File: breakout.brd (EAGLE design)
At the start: 25.4 x 32.4 mm, 11 parts, among them IC2 REG1117

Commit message: Tidy up for publishing
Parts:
- added FRAME1: (no value), SparkFun-Aesthetics:DUMMY
- added LOGO1: OSHW-LOGOS, SparkFun-Aesthetics:OSHW-LOGO-S
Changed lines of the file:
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@@
 <layer number="112" name="tSilk" color="7" fill="1" visible="yes" active="yes"/>
 <layer number="113" name="IDFDebug" color="4" fill="1" visible="yes" active="yes"/>
+<layer number="114" name="FRNTMAAT1" color="7" fill="1" visible="yes" active="yes"/>
+<layer number="115" name="FRNTMAAT2" color="7" fill="1" visible="yes" active="yes"/>
 <layer number="116" name="Patch_BOT" color="9" fill="4" visible="no" active="yes"/>
+<layer number="117" name="BACKMAAT1" color="7" fill="1" visible="yes" active="yes"/>
+<layer number="118" name="Rect_Pads" color="7" fill="1" visible="no" active="no"/>
+<layer number="119" name="KAP_TEKEN" color="7" fill="1" visible="yes" active="yes"/>
+<layer number="120" name="KAP_MAAT1" color="7" fill="1" visible="yes" active="yes"/>
 <layer number="121" name="_tsilk" color="7" fill="1" visible="no" active="yes"/>
 <layer number="122" name="_bsilk" color="7" fill="1" visible="no" active="yes"/>
@@
 <layer number="128" name="_bValues" color="7" fill="1" visible="yes" active="yes"/>
 <layer number="129" name="Mask" color="7" fill="1" visible="yes" active="yes"/>
+<layer number="130" name="SMDSTROOK" color="7" fill="1" visible="yes" active="yes"/>
 <layer number="131" name="tAdjust" color="7" fill="1" visible="yes" active="yes"/>
 <layer number="132" name="bAdjust" color="7" fill="1" visible="yes" active="yes"/>
@@
 <layer number="230" name="230bmp" color="7" fill="1" visible="yes" active="yes"/>
 <layer number="231" name="231bmp" color="7" fill="1" visible="yes" active="yes"/>
+<layer number="232" name="Eagle3D_PG2" color="7" fill="1" visible="no" active="no"/>
+<layer number="233" name="Eagle3D_PG3" color="7" fill="1" visible="no" active="no"/>
 <layer number="248" name="Housing" color="7" fill="1" visible="yes" active="yes"/>
 <layer number="249" name="Edge" color="7" fill="1" visible="yes" active="yes"/>
@@
 <attribute name="VALUE" x="12.065" y="27.6225" size="1.778" layer="27" ratio="10" rot="R270"/>
 </element>
-<element name="MDL1" library="ESP8266-ESP12E" package="ESP8266-ESP12E" value="" x="4.445" y="8.255"/>
+<element name="MDL1" library="ESP8266-ESP12E" package="ESP8266-ESP12E" value="" x="4.445" y="8.255" smashed="yes"/>
 <element name="C1" library="SparkFun-Capacitors" package="1206" value="0.1uf" x="7.3025" y="3.4925" smashed="yes" rot="R90">
-<attribute name="NAME" x="6.985" y="6.06425" size="0.4064" layer="25"/>
-<attribute name="VALUE" x="8.8265" y="2.0955" size="0.4064" layer="27" rot="R90"/>
+<attribute name="NAME" x="6.6675" y="6.06425" size="0.8128" layer="25"/>
 </element>
 <element name="C2" library="SparkFun-Capacitors" package="1206" value="0.1uf" x="5.08" y="3.4925" smashed="yes" rot="R90">
-<attribute name="NAME" x="4.7625" y="6.06425" size="0.4064" layer="25"/>
-<attribute name="VALUE" x="6.604" y="2.0955" size="0.4064" layer="27" rot="R90"/>
+<attribute name="NAME" x="4.445" y="6.06425" size="0.8128" layer="25"/>
 </element>
 <element name="IC2" library="burr-brown" package="SOT223" value="REG1117" x="13.0175" y="3.4925" smashed="yes" rot="R270">
@@
 </element>
 <element name="PWR" library="SparkFun-LED" package="LED-1206" value="" x="21.2725" y="3.175" smashed="yes" rot="R270">
-<attribute name="NAME" x="20.54225" y="5.842" size="0.4064" layer="25"/>
+<attribute name="NAME" x="19.90725" y="5.842" size="0.8128" layer="25"/>
 <attribute name="VALUE" x="19.4945" y="4.191" size="0.4064" layer="27" rot="R270"/>
 </element>
 <element name="R1" library="SparkFun-Resistors" package="1206" value="220Ohm" x="18.89125" y="3.175" smashed="yes" rot="R270">
-<attribute name="NAME" x="18.57375" y="5.9055" size="0.4064" layer="25"/>
-</element>
-<element name="R2" library="SparkFun-Resistors" package="1206" value="10k" x="5.3975" y="30.1625" rot="MR0"/>
-<element name="R3" library="SparkFun-Resistors" package="1206" value="10k" x="5.55625" y="25.0825" rot="MR0"/>
-<element name="R4" library="SparkFun-Resistors" package="1206" value="10k" x="19.84375" y="20.0025" rot="MR180"/>
-<element name="R5" library="SparkFun-Resistors" package="1206" value="10k" x="20.0025" y="14.9225" rot="MR180"/>
+<attribute name="NAME" x="18.0975" y="5.9055" size="0.8128" layer="25"/>
+</element>
+<element name="R2" library="SparkFun-Resistors" package="1206" value="10k" x="5.3975" y="30.1625" smashed="yes" rot="MR0">
+<attribute name="NAME" x="8.128" y="29.5275" size="0.8128" layer="26" rot="MR90"/>
+</element>
+<element name="R3" library="SparkFun-Resistors" package="1206" value="10k" x="5.55625" y="25.0825" smashed="yes" rot="MR0">
+<attribute name="NAME" x="8.28675" y="24.4475" size="0.8128" layer="26" rot="MR90"/>
+</element>
+<element name="R4" library="SparkFun-Resistors" package="1206" value="10k" x="19.84375" y="20.0025" smashed="yes" rot="MR180">
+<attribute name="NAME" x="17.11325" y="20.47875" size="0.8128" layer="26" rot="MR270"/>
+</element>
+<element name="R5" library="SparkFun-Resistors" package="1206" value="10k" x="20.0025" y="14.9225" smashed="yes" rot="MR180">
+<attribute name="NAME" x="17.272" y="15.39875" size="0.8128" layer="26" rot="MR270"/>
+</element>
+<element name="LOGO1" library="SparkFun-Aesthetics" package="OSHW-LOGO-S" value="OSHW-LOGOS" x="18.415" y="28.8925" smashed="yes" rot="MR0"/>
+<element name="FRAME1" library="SparkFun-Aesthetics" package="DUMMY" value="" x="0.3175" y="-4.28625">
+<attribute name="VERSION" value="v01" x="-0.635" y="-3.175" size="1.778" layer="27" display="off"/>
+<attribute name="DESIGNER" value="Nobody" x="-0.635" y="-3.175" size="1.778" layer="27" display="off"/>
+</element>
 </elements>
 <signals>

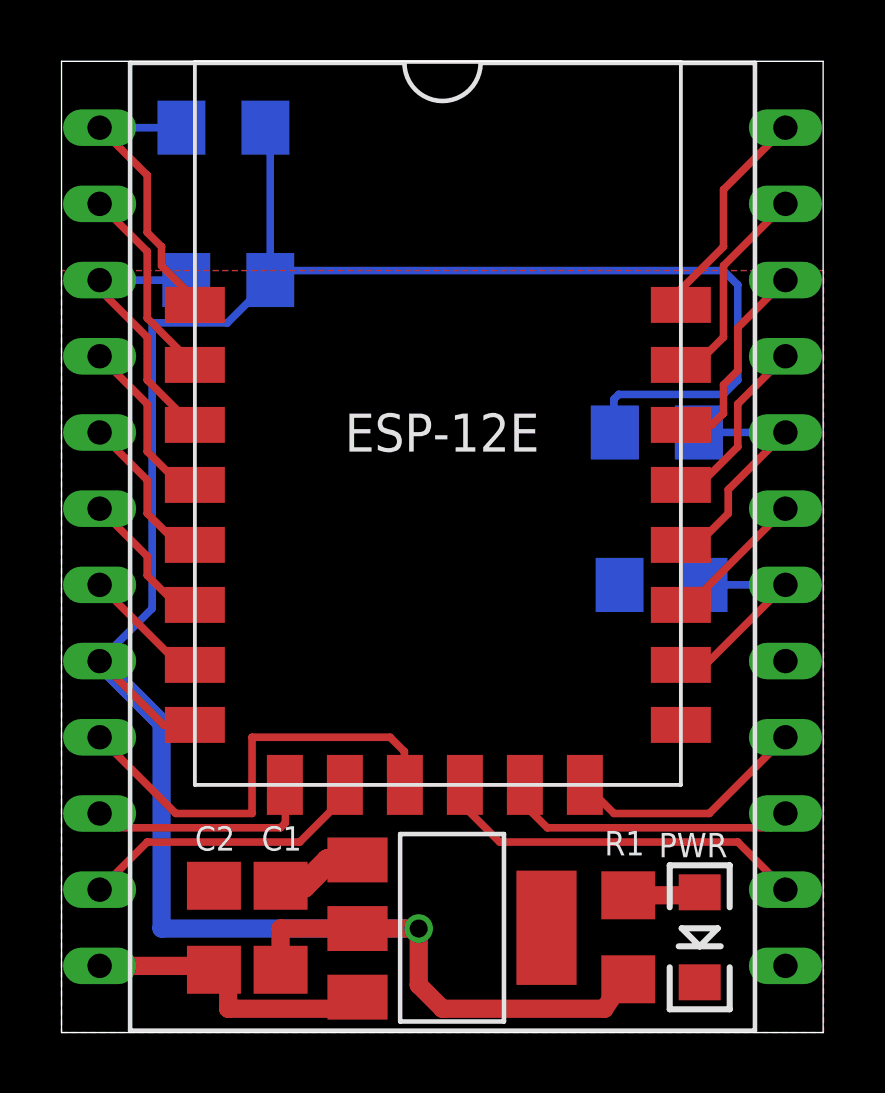
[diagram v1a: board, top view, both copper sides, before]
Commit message: Added FTDI + USB support on the board. Also cleaned up the schematic. DRC pass.
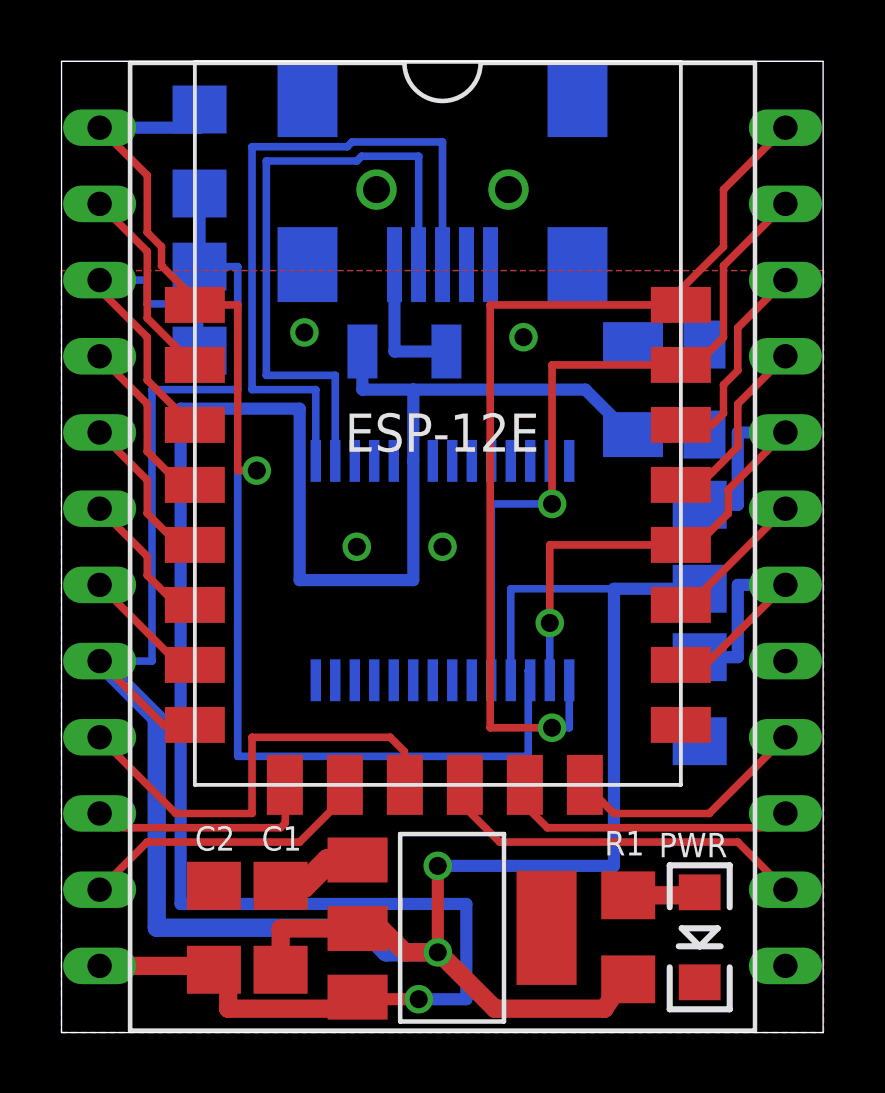
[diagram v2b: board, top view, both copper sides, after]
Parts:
- added C5: 0.1uF, rcl:C1206K
- added C6: 10uF, rcl:SMC_A
- added F1: 500mA, SparkFun:PTC-1206
- added U4: FT232R, SparkFun:SSOP28DB
- added USB: USB-SMD-NS, SparkFun-Connectors:USB-MINIB-NOSTOP
- moved R4 4.07 mm to (21.3, 16.2), turned to 90 degrees
- moved R5 4.02 mm to (21.3, 11.1), turned to 90 degrees
- moved LOGO1 1.75 mm to (20.2, 28.9)
- moved R3 1.35 mm to (4.60, 24.1), turned to 270 degrees
- moved R2 1.12 mm to (4.60, 29.4), turned to 90 degrees
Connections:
- new net CTS: U4.11
- new net DCD: U4.10
- new net DSR: U4.9
- new net PWREN: U4.14
- new net RI: U4.6
- new net SLEEP: U4.12
- new net TXDEN: U4.13
- new net USB_D+: U4.15, USB.D+
- new net USB_D-: U4.16, USB.D-
- new net USB_VIN: F1.1, USB.VBUS
- net 3.3V: now also U4.4
- net 5V: now also C5.1, C6.+, F1.2, U4.20
- net GND: now also C5.2, C6.-, U4.18, U4.21, U4.25, U4.26, U4.7, USB.GND
- net GPIO0: now also U4.2
- net RESET: now also U4.3
- net RX: now also U4.5
- net TX: now also U4.1
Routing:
- net 5V: track 10.4 -> 76.6 mm, vias 0 -> 1
- net RESET: track 9.95 -> 41.8 mm, vias 0 -> 1
- net TX: track 7.35 -> 32.0 mm, vias 0 -> 1
- net USB_D+: track 0.00 -> 23.1 mm
- net USB_D-: track 0.00 -> 21.1 mm
- net RX: track 7.10 -> 23.9 mm, vias 0 -> 1
- net GPIO0: track 8.39 -> 19.7 mm, vias 0 -> 1
- net USB_VIN: track 0.00 -> 4.63 mm
- net CH_PD: track 9.08 -> 11.9 mm
- net GPIO15: track 7.32 -> 9.86 mm
- net 3.3V: track 84.4 -> 86.8 mm, vias 1 -> 2
- net GND: vias 0 -> 4

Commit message: Slight revision to the GND plane.
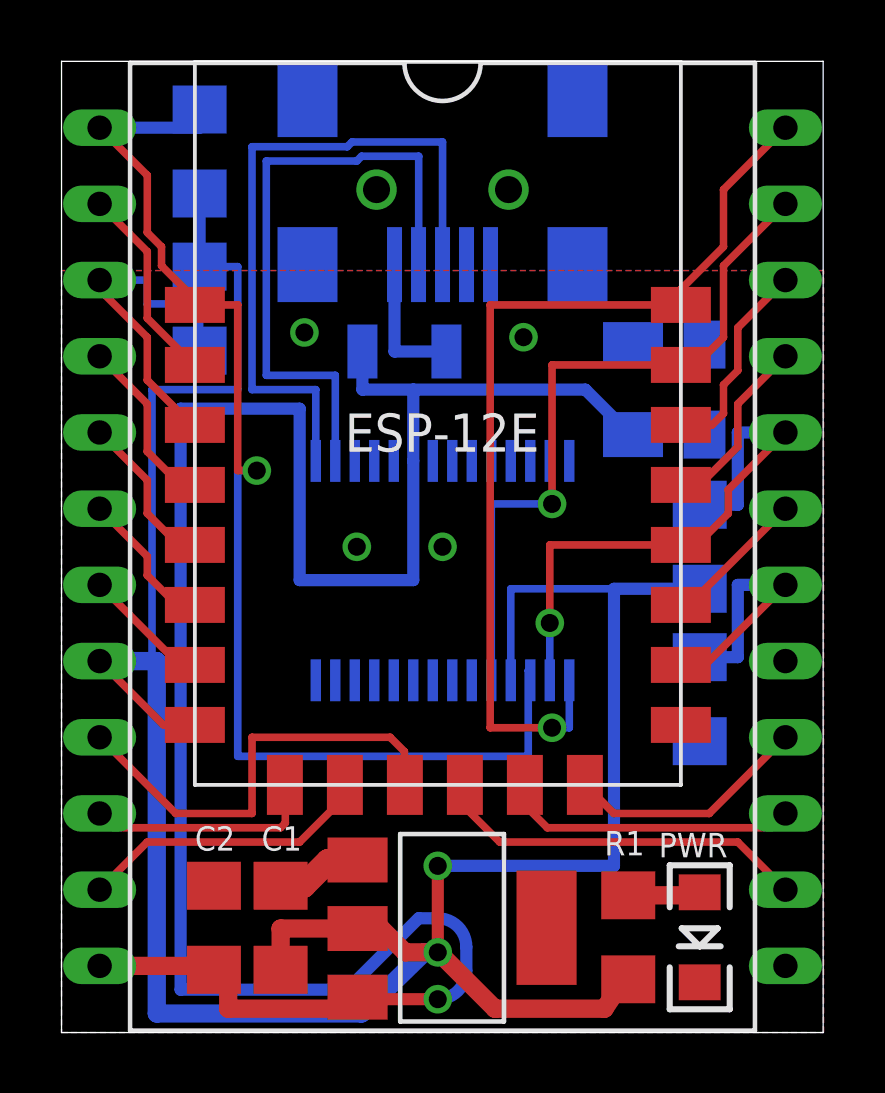
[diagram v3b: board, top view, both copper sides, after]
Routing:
- net 3.3V: track 86.8 -> 91.3 mm
- net 5V: track 76.6 -> 78.7 mm
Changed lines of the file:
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@@
 <contactref element="IC2" pad="3"/>
 <contactref element="C2" pad="1"/>
-<wire x1="9.8679" y1="1.1811" x2="9.8679" y2="0.79375" width="0.6096" layer="1"/>
+<wire x1="9.8679" y1="1.1811" x2="9.8679" y2="1.11125" width="0.6096" layer="1"/>
+<wire x1="9.8679" y1="1.11125" x2="9.8679" y2="0.79375" width="0.6096" layer="1"/>
 <wire x1="9.8679" y1="0.79375" x2="5.55625" y2="0.79375" width="0.6096" layer="1"/>
 <wire x1="5.55625" y1="0.79375" x2="5.55625" y2="2.0925" width="0.6096" layer="1"/>
@@
 <wire x1="7.9375" y1="15.08125" x2="7.9375" y2="20.79625" width="0.4064" layer="16"/>
 <wire x1="7.9375" y1="20.79625" x2="3.96875" y2="20.79625" width="0.4064" layer="16"/>
-<wire x1="3.96875" y1="20.79625" x2="3.96875" y2="4.28625" width="0.4064" layer="16"/>
-<wire x1="3.96875" y1="4.28625" x2="13.49375" y2="4.28625" width="0.4064" layer="16"/>
-<wire x1="13.49375" y1="4.28625" x2="13.49375" y2="1.11125" width="0.4064" layer="16"/>
-<wire x1="13.49375" y1="1.11125" x2="11.90625" y2="1.11125" width="0.4064" layer="16"/>
-<via x="11.90625" y="1.11125" extent="1-16" drill="0.6"/>
-<wire x1="11.90625" y1="1.11125" x2="9.8679" y2="1.11125" width="0.4064" layer="1"/>
-<wire x1="9.8679" y1="1.11125" x2="9.8679" y2="1.1811" width="0.4064" layer="1"/>
+<wire x1="3.96875" y1="20.79625" x2="3.96875" y2="1.42875" width="0.4064" layer="16"/>
+<wire x1="3.96875" y1="1.42875" x2="9.525" y2="1.42875" width="0.4064" layer="16"/>
+<wire x1="9.525" y1="1.42875" x2="11.90625" y2="3.81" width="0.4064" layer="16"/>
+<via x="12.54125" y="1.11125" extent="1-16" drill="0.6"/>
+<wire x1="12.54125" y1="1.11125" x2="9.8679" y2="1.11125" width="0.4064" layer="1"/>
+<wire x1="11.90625" y1="3.81" x2="12.54125" y2="3.81" width="0.4064" layer="16"/>
+<wire x1="12.54125" y1="3.81" x2="13.49375" y2="2.8575" width="0.4064" layer="16" curve="-90"/>
+<wire x1="13.49375" y1="2.8575" x2="13.49375" y2="2.06375" width="0.4064" layer="16"/>
+<wire x1="12.54125" y1="1.11125" x2="13.49375" y2="2.06375" width="0.4064" layer="16" curve="90"/>
 </signal>
 <signal name="GPIO12">
@@
 <wire x1="7.3025" y1="2.0925" x2="7.3025" y2="3.4671" width="0.6096" layer="1"/>
 <wire x1="7.3025" y1="3.4671" x2="9.8679" y2="3.4671" width="0.6096" layer="1"/>
-<wire x1="1.27" y1="12.3825" x2="3.175" y2="10.4775" width="0.6096" layer="16"/>
-<wire x1="3.175" y1="10.4775" x2="3.175" y2="3.4925" width="0.6096" layer="16"/>
+<wire x1="3.175" y1="12.3825" x2="3.175" y2="0.635" width="0.6096" layer="16"/>
 <wire x1="9.8679" y1="3.4671" x2="10.63625" y2="3.4925" width="0.6096" layer="1"/>
 <wire x1="10.63625" y1="3.4925" x2="11.4554" y2="2.67335" width="0.6096" layer="1"/>
 <wire x1="11.4554" y1="2.67335" x2="12.54125" y2="2.67335" width="0.6096" layer="1"/>
 <via x="12.54125" y="2.67335" extent="1-16" drill="0.6"/>
-<wire x1="12.54125" y1="2.67335" x2="10.8204" y2="2.67335" width="0.6096" layer="16"/>
-<wire x1="10.8204" y1="2.67335" x2="10.00125" y2="3.4925" width="0.6096" layer="16"/>
-<wire x1="10.00125" y1="3.4925" x2="3.175" y2="3.4925" width="0.6096" layer="16"/>
+<wire x1="12.54125" y1="2.67335" x2="12.0904" y2="2.67335" width="0.6096" layer="16"/>
+<wire x1="12.0904" y1="2.67335" x2="10.00125" y2="0.635" width="0.6096" layer="16"/>
+<wire x1="10.00125" y1="0.635" x2="3.175" y2="0.635" width="0.6096" layer="16"/>
 <wire x1="4.445" y1="10.255" x2="3.3975" y2="10.255" width="0.254" layer="1"/>
 <wire x1="3.3975" y1="10.255" x2="1.27" y2="12.3825" width="0.254" layer="1"/>
@@
 <wire x1="18.415" y1="5.55625" x2="18.415" y2="14.7925" width="0.4064" layer="16"/>
 <wire x1="4.60375" y1="25.53" x2="4.60375" y2="27.96875" width="0.4064" layer="16"/>
+<wire x1="3.175" y1="12.3825" x2="1.27" y2="12.3825" width="0.6096" layer="16"/>
 </signal>
 <signal name="GPIO13">

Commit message: Revision to switch around TX/RX lines so that this thing actually works, detach RTS signal from RESET, add TX & RX LEDs + assoc. resistors. Renamed GPIO4 & GPIO5 as SDA and SCL respectively to suit their default i2c states.
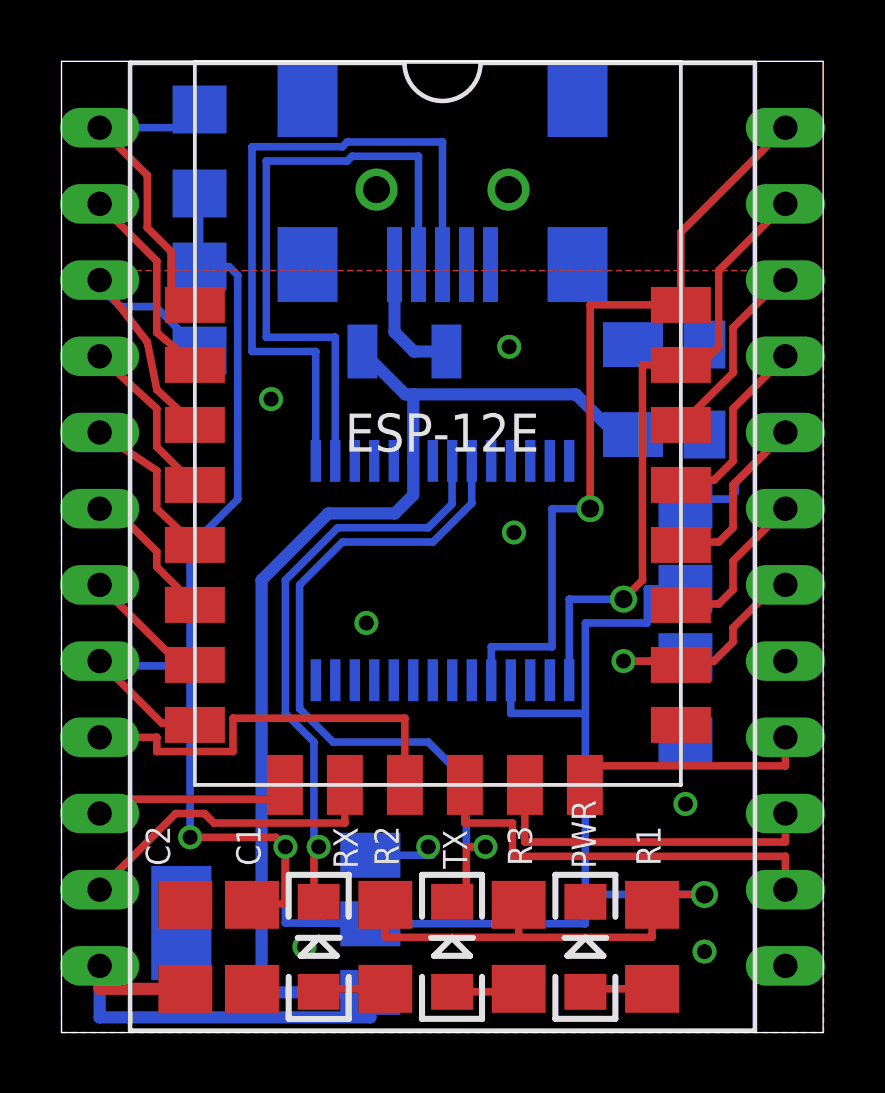
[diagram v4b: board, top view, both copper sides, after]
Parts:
- added R6, R7: 10k, SparkFun-Resistors:1206
- added RX: RED, SparkFun-LED:LED-1206
- added TX: GREEN, SparkFun-LED:LED-1206
- R1: value 220Ohm -> 330Ohm
- R2, R3: value 10k -> 330; device SparkFun-Resistors:1206 -> SparkFun-Passives:1206
- moved R2 27.2 mm to (10.8, 2.86), flipped to the top
- moved R3 23.8 mm to (15.2, 2.86), flipped to the top, turned to 90 degrees
- moved R4 21.2 mm to (4.60, 29.4)
- moved R5 21.1 mm to (4.60, 24.1), turned to 270 degrees
- moved IC2 5.88 mm to (7.14, 3.65), flipped to the bottom
- moved PWR 3.82 mm to (17.5, 2.86), turned to 90 degrees
- moved C1 1.14 mm to (6.35, 2.86), turned to 270 degrees
- moved C2 1.14 mm to (4.13, 2.86)
- moved R1 0.85 mm to (19.7, 2.86), turned to 90 degrees
- renumbered C5 to C3, C6 to C4
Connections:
- net GPIO4 renamed SDA
- net GPIO5 renamed SCL
- removed net CTS: U4.11
- removed net DCD: U4.10
- removed net DSR: U4.9
- removed net RI: U4.6
- new net N$2: R2.1, RX.A
- new net N$3: R3.1, TX.A
- new net RXLED: RX.C, U4.22
- new net TXLED: TX.C, U4.23
- net 3.3V: now also R2.2, R3.2, R5.1, R6.1; no longer R2.1, R3.1
- net CH_PD: now also R5.2; no longer R3.2
- net GND: now also R7.1; no longer R5.1
- net GPIO0: now also R6.2; no longer R4.2, U4.2
- net GPIO15: now also R7.2; no longer R5.2
- net RESET: now also R4.2; no longer R2.2, U4.3
- net RX: now also U4.1; no longer U4.5
- net TX: now also U4.5; no longer U4.1
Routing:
- net RESET: track 41.8 -> 10.9 mm, vias 1 -> 0
- net TXLED: track 0.00 -> 24.8 mm, vias 0 -> 1
- net 5V: track 78.7 -> 54.7 mm, vias 1 -> 0
- net RXLED: track 0.00 -> 19.6 mm, vias 0 -> 1
- net GPIO0: track 19.7 -> 10.4 mm, vias 1 -> 0
- net TX: track 32.0 -> 26.2 mm
- net 3.3V: track 91.3 -> 86.0 mm, vias 2 -> 3
- net RX: track 23.9 -> 21.1 mm
- net N$3: track 0.00 -> 2.32 mm
- net N$2: track 0.00 -> 2.32 mm
- net CS0: track 9.87 -> 11.5 mm
- net SCLK: track 12.6 -> 14.2 mm
- net CH_PD: track 11.9 -> 10.4 mm
- net MOSI: track 15.1 -> 14.0 mm
- net GPIO15: track 9.86 -> 9.03 mm, vias 0 -> 1
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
